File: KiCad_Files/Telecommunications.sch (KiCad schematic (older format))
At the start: 23 parts, among them IC1 L7806ABD2T-TR, J4 CONSMA001-SMD-G, J5 CONSMA001-SMD-G, J6 U_FL-R-SMT_10_, J7 CONSMA001-SMD-G, U2 2AD66-1262, U3 LoRa1262F30, U5 NEO-M8N

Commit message: Add shapes3D folder
Now all 3D models for the components are stored in a single folder, thanks to the Archive Plugin from https://github.com/MitjaNemec/Kicad_action_plugins.git
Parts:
- BT1: symbol Caurin-v.2.0-rescue:ML414H_IV01E-ML414H_IV01E -> archive:Caurin-v.2.0-rescue_ML414H_IV01E-ML414H_IV01E
- C11, C12, C13, C14, C15, C16, C17: symbol Device:C_Small -> archive:Device_C_Small
- D2: symbol Device:D_Schottky_Small -> archive:Device_D_Schottky_Small
- IC1: symbol SamacSys_Parts:L7806ABD2T-TR -> archive:SamacSys_Parts_L7806ABD2T-TR
- J4, J5, J7: symbol dk_Coaxial-Connectors-RF:CONSMA001-SMD-G -> archive:dk_Coaxial-Connectors-RF_CONSMA001-SMD-G
- J6: symbol dk_Coaxial-Connectors-RF:U_FL-R-SMT_10_ -> archive:dk_Coaxial-Connectors-RF_U_FL-R-SMT_10_
- JP2: symbol Jumper:SolderJumper_3_Open -> archive:Jumper_SolderJumper_3_Open
- L1: symbol Device:L_Small -> archive:Device_L_Small
- R5, R6, R7, R8: symbol Device:R_Small -> archive:Device_R_Small
- U2: symbol RF_Modules_Zenith:2AD66-1262 -> archive:RF_Modules_Zenith_2AD66-1262
- U3: symbol RF_Modules_Zenith:LoRa1262F30 -> archive:RF_Modules_Zenith_LoRa1262F30
- U5: symbol Zenith_Modified_Libraries:NEO-M8N -> archive:Zenith_Modified_Libraries_NEO-M8N
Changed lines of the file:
@@
 	9650 4450 9550 4450
 $Comp
-L power:GND #PWR0121
+L archive:power_GND #PWR0121
 U 1 1 60E173C8
 P 8850 5150
@@
 $EndComp
 $Comp
-L power:GND #PWR0122
+L archive:power_GND #PWR0122
 U 1 1 60E17945
 P 9050 2800
@@
 	9050 2700 9050 2800
 $Comp
-L power:+3V3 #PWR0123
+L archive:power_+3V3 #PWR0123
 U 1 1 60E187D2
 P 7700 3150
@@
 $EndComp
 $Comp
-L power:GND #PWR0124
+L archive:power_GND #PWR0124
 U 1 1 60E19D9C
 P 7700 3550
@@
 $EndComp
 $Comp
-L Device:C_Small C15
+L archive:Device_C_Small C15
 U 1 1 60E1A4E4
 P 7700 3400
@@
 NoConn ~ 9550 4150
 $Comp
-L Device:L_Small L1
+L archive:Device_L_Small L1
 U 1 1 60E57109
 P 9875 3375
@@
 	9875 3100 9875 3275
 $Comp
-L Device:R_Small R8
+L archive:Device_R_Small R8
 U 1 1 60E5B23B
 P 9400 3100
@@
 $EndComp
 $Comp
-L Device:C_Small C17
+L archive:Device_C_Small C17
 U 1 1 60E5C8AF
 P 10250 3250
@@
 	4925 3000 4875 3000
 $Comp
-L power:+5V #PWR?
+L archive:power_+5V #PWR?
 U 1 1 60FC2EF1
 P 2600 2050
@@
 	6950 6500 6950 500
 $Comp
-L Caurin-v.2.0-rescue:ML414H_IV01E-ML414H_IV01E BT?
+L archive:Caurin-v.2.0-rescue_ML414H_IV01E-ML414H_IV01E BT?
 U 1 1 6116FC93
 P 8500 2500
@@
 $EndComp
 $Comp
-L Device:C_Small C16
+L archive:Device_C_Small C16
 U 1 1 61171146
 P 8450 2800
@@
 $EndComp
 $Comp
-L Device:R_Small R7
+L archive:Device_R_Small R7
 U 1 1 6117170F
 P 8750 2300
@@
 $EndComp
 $Comp
-L power:+3V3 #PWR0129
+L archive:power_+3V3 #PWR0129
 U 1 1 61172368
 P 8750 1900
@@
 $EndComp
 $Comp
-L power:GND #PWR0130
+L archive:power_GND #PWR0130
 U 1 1 61172B25
 P 8150 2900
@@
 	8750 2500 8700 2500
 $Comp
-L Device:D_Schottky_Small D2
+L archive:Device_D_Schottky_Small D2
 U 1 1 61179C6F
 P 8750 2050
@@
 GPS_TX
 $Comp
-L Device:C_Small C14
+L archive:Device_C_Small C14
 U 1 1 61451F4E
 P 3075 2550
@@
 $EndComp
 $Comp
-L RF_Modules_Zenith:LoRa1262F30 U3
+L archive:RF_Modules_Zenith_LoRa1262F30 U3
 U 1 1 614691E3
 P 4425 2100
@@
 	500  4325 6950 4325
 $Comp
-L RF_Modules_Zenith:2AD66-1262 U2
+L archive:RF_Modules_Zenith_2AD66-1262 U2
 U 1 1 614C66F0
 P 3575 5575
@@
 RADIOS_MISO
 $Comp
-L power:GND #PWR?
+L archive:power_GND #PWR?
 U 1 1 614E9798
 P 3075 2725
@@
 RADIO1_NSS
 $Comp
-L Device:R_Small R5
+L archive:Device_R_Small R5
 U 1 1 61512324
 P 4275 5725
@@
 $EndComp
 $Comp
-L power:+3V3 #PWR0132
+L archive:power_+3V3 #PWR0132
 U 1 1 6151232B
 P 4275 5575
@@
 	4275 5575 4275 5625
 $Comp
-L Device:R_Small R6
+L archive:Device_R_Small R6
 U 1 1 61514E9B
 P 5000 2200
@@
 $EndComp
 $Comp
-L power:+3V3 #PWR0133
+L archive:power_+3V3 #PWR0133
 U 1 1 61514EA2
 P 5000 2075
@@
 	4175 5975 5050 5975
 $Comp
-L Device:C_Small C13
+L archive:Device_C_Small C13
 U 1 1 61544A14
 P 2825 5725
@@
 $EndComp
 $Comp
-L power:GND #PWR?
+L archive:power_GND #PWR?
 U 1 1 61544A1A
 P 2825 5875
@@
 	2825 5825 2825 5875
 $Comp
-L power:+3V3 #PWR0135
+L archive:power_+3V3 #PWR0135
 U 1 1 615473DA
 P 2825 5525
@@
 	3875 2800 3975 2800
 $Comp
-L power:GND #PWR?
+L archive:power_GND #PWR?
 U 1 1 6155871A
 P 4425 3525
@@
 	2975 6275 3075 6275
 $Comp
-L power:GND #PWR?
+L archive:power_GND #PWR?
 U 1 1 6157989A
 P 3625 6975
@@
 	3725 6900 3725 6825
 $Comp
-L SamacSys_Parts:L7806ABD2T-TR IC1
+L archive:SamacSys_Parts_L7806ABD2T-TR IC1
 U 1 1 61E126D4
 P 1975 2875
@@
 $EndComp
 $Comp
-L Device:C_Small C11
+L archive:Device_C_Small C11
 U 1 1 61E1B6CC
 P 1400 3075
@@
 $EndComp
 $Comp
-L Device:C_Small C12
+L archive:Device_C_Small C12
 U 1 1 61E1C718
 P 2600 3075
@@
 $EndComp
 $Comp
-L power:GND #PWR?
+L archive:power_GND #PWR?
 U 1 1 61E1D31F
 P 1975 3375
@@
 	1975 3375 1975 3325
 $Comp
-L Jumper:SolderJumper_3_Open JP2
+L archive:Jumper_SolderJumper_3_Open JP2
 U 1 1 61E5B8C3
 P 2600 2350
@@
 	4175 6375 4225 6375
 $Comp
-L dk_Coaxial-Connectors-RF:CONSMA001-SMD-G J4
+L archive:dk_Coaxial-Connectors-RF_CONSMA001-SMD-G J4
 U 1 1 624D77E2
 P 5200 5875
@@
 $EndComp
 $Comp
-L dk_Coaxial-Connectors-RF:CONSMA001-SMD-G J5
+L archive:dk_Coaxial-Connectors-RF_CONSMA001-SMD-G J5
 U 1 1 624E0650
 P 5875 2350
@@
 $EndComp
 $Comp
-L power:+BATT #PWR0153
+L archive:power_+BATT #PWR0153
 U 1 1 6154AA35
 P 1400 2700
@@
 	1400 2875 1400 2975
 $Comp
-L Zenith_Modified_Libraries:NEO-M8N U5
+L archive:Zenith_Modified_Libraries_NEO-M8N U5
 U 1 1 615EB70D
 P 8850 4150
@@
 	10750 3900 10750 3950
 $Comp
-L dk_Coaxial-Connectors-RF:CONSMA001-SMD-G J7
+L archive:dk_Coaxial-Connectors-RF_CONSMA001-SMD-G J7
 U 1 1 624E5195
 P 10750 4300
@@
 $EndComp
 $Comp
-L dk_Coaxial-Connectors-RF:U_FL-R-SMT_10_ J6
+L archive:dk_Coaxial-Connectors-RF_U_FL-R-SMT_10_ J6
 U 1 1 613F91A3
 P 10750 3700
@@
 	10750 4550 10750 4500
 $Comp
-L power:GNDA #PWR0125
+L archive:power_GNDA #PWR0125
 U 1 1 6160D822
 P 10750 3950
@@
 $EndComp
 $Comp
-L power:GNDA #PWR0126
+L archive:power_GNDA #PWR0126
 U 1 1 6160DC19
 P 10750 4550
@@
 $EndComp
 $Comp
-L power:GNDA #PWR0127
+L archive:power_GNDA #PWR0127
 U 1 1 6160DE64
 P 10250 3400
@@
 $EndComp
 $Comp
-L power:GNDA #PWR0154
+L archive:power_GNDA #PWR0154
 U 1 1 6160E139
 P 9625 3850

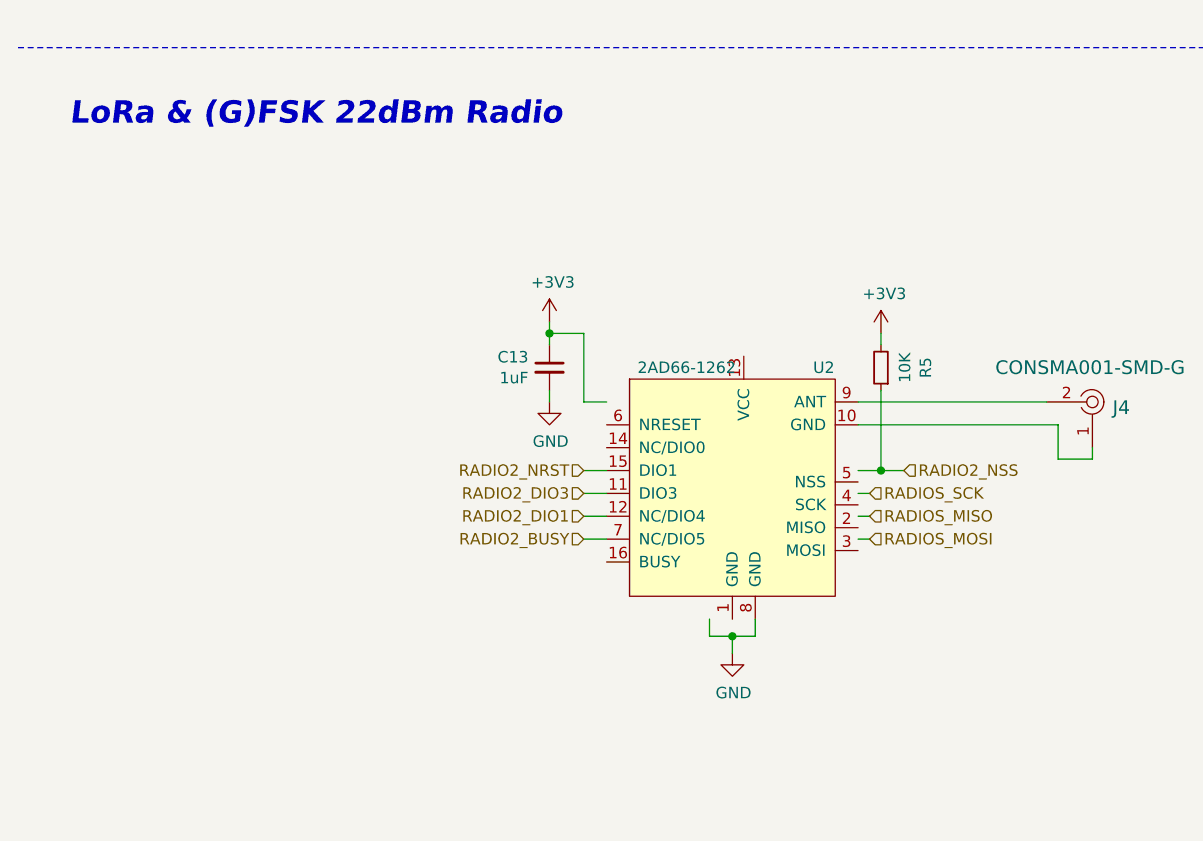
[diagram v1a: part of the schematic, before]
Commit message: Add solder jumper for DIO pins.
Adds solder jumper for DIO pin compatibility between SX1276 and SX1262 low power radios.
Also added the name of the designer (me).
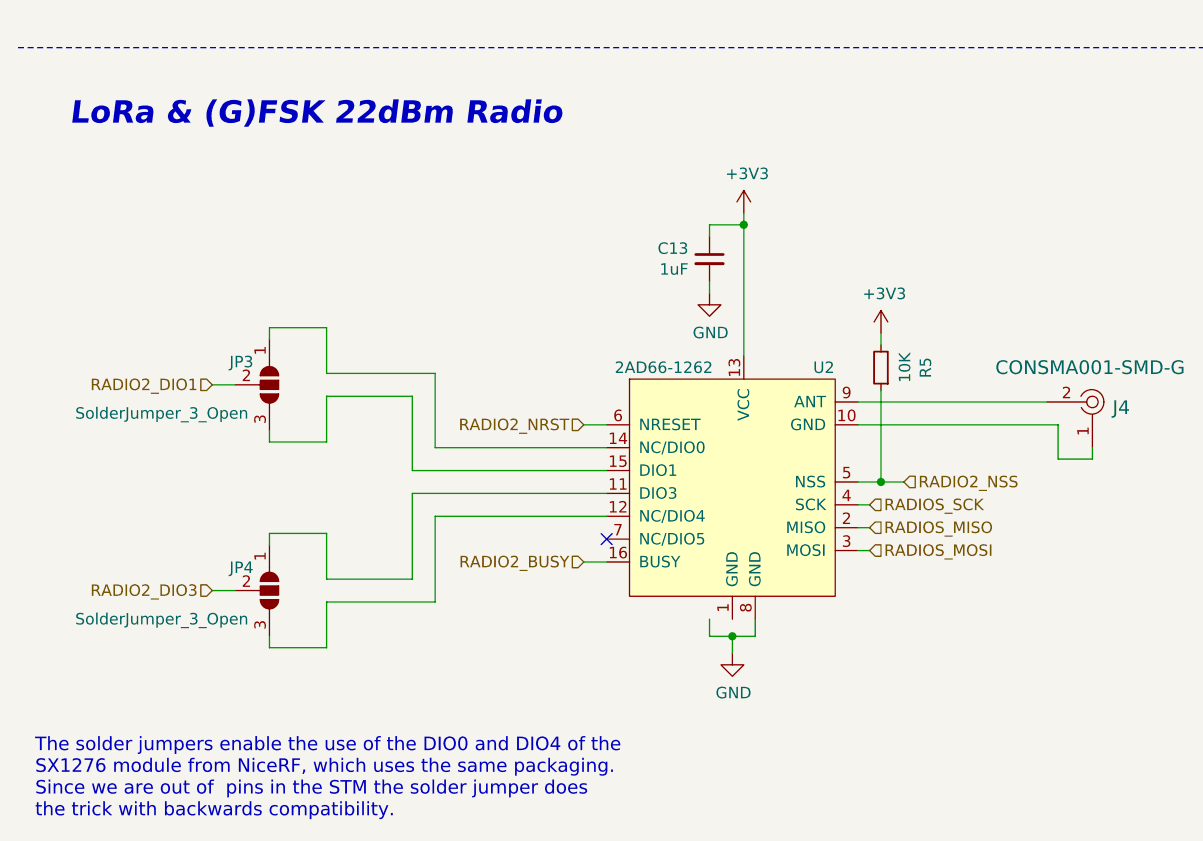
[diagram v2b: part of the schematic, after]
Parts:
- added JP3, JP4: SolderJumper_3_Open, Caurin_Footprints:SolderJumper-3_P1.3mm_Open_RoundedPad1.0x1.5mm_NumberLabels, symbol Jumper:SolderJumper_3_Open
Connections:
- wire segments 113 -> 136
- no-connect marks 7 -> 8
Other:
- note added: "The solder jumpers enable the use of the DIO0 and DIO4 of the\nSX1276 module from NiceRF, which uses the same packaging.\nSince we are out of pins in the STM the solder jumper does\nthe trick with backwards compatibility."
- moved on the sheet: C13
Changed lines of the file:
@@
 Wire Notes Line
 	500  4325 6950 4325
-$Comp
-L archive:RF_Modules_Zenith_2AD66-1262 U2
-U 1 1 614C66F0
-P 3575 5575
-F 0 "U2" H 4025 5425 50  0000 C CNN
-F 1 "2AD66-1262" H 3425 5425 50  0000 C CNN
-F 2 "RF_Modules_Zenith:2AD66-126x" H 3975 5425 50  0001 C CNN
-F 3 "" H 3975 5425 50  0001 C CNN
-	1    3575 5575
-	1    0    0    -1
-$EndComp
 Wire Wire Line
 	4875 2900 4925 2900
 Text HLabel 4925 2900 2    50   Input ~ 0
 RADIOS_MISO
-Text HLabel 4225 6475 2    50   Input ~ 0
+Text HLabel 4225 6525 2    50   Input ~ 0
 RADIOS_MOSI
 Wire Wire Line
-	4225 6475 4175 6475
-Text HLabel 4225 6275 2    50   Input ~ 0
+	4225 6525 4175 6525
+Text HLabel 4225 6325 2    50   Input ~ 0
 RADIOS_SCK
 Wire Wire Line
-	4175 6275 4225 6275
-Text HLabel 4225 6375 2    50   Input ~ 0
+	4175 6325 4225 6325
+Text HLabel 4225 6425 2    50   Input ~ 0
 RADIOS_MISO
 $Comp
@@
 Wire Wire Line
 	5000 2700 5100 2700
-Text HLabel 4375 6175 2    50   Input ~ 0
-RADIO2_NSS
-Wire Wire Line
-	4175 6175 4275 6175
-Wire Wire Line
-	4275 5825 4275 6175
-Wire Wire Line
-	4275 6175 4375 6175
-Connection ~ 4275 6175
-Wire Wire Line
-	5000 5875 4175 5875
 Wire Wire Line
 	5050 5975 5050 6125
@@
 L archive:Device_C_Small C13
 U 1 1 61544A14
-P 2825 5725
-F 0 "C13" H 2917 5771 50  0000 L CNN
-F 1 "1uF" H 2917 5680 50  0000 L CNN
-F 2 "Capacitor_SMD:C_0805_2012Metric" H 2825 5725 50  0001 C CNN
-F 3 "~" H 2825 5725 50  0001 C CNN
-	1    2825 5725
+P 3525 5250
+F 0 "C13" H 3617 5296 50  0000 L CNN
+F 1 "1uF" H 3617 5205 50  0000 L CNN
+F 2 "Capacitor_SMD:C_0805_2012Metric" H 3525 5250 50  0001 C CNN
+F 3 "~" H 3525 5250 50  0001 C CNN
+	1    3525 5250
 	-1   0    0    -1
 $EndComp
@@
 L archive:power_GND #PWR?
 U 1 1 61544A1A
-P 2825 5875
+P 3525 5400
 AR Path="/60D267AF/61544A1A" Ref="#PWR?"  Part="1"
 AR Path="/60D892C4/61544A1A" Ref="#PWR?"  Part="1"
 AR Path="/613F33BD/61544A1A" Ref="#PWR0134"  Part="1"
-F 0 "#PWR0134" H 2825 5625 50  0001 C CNN
-F 1 "GND" H 2830 5702 50  0000 C CNN
-F 2 "" H 2825 5875 50  0001 C CNN
-F 3 "" H 2825 5875 50  0001 C CNN
-	1    2825 5875
-	1    0    0    -1
-$EndComp
-Wire Wire Line
-	2825 5575 2975 5575
-Wire Wire Line
-	2975 5575 2975 5875
-Wire Wire Line
-	2975 5875 3075 5875
-Connection ~ 2825 5575
-Wire Wire Line
-	2825 5575 2825 5625
-Wire Wire Line
-	2825 5825 2825 5875
+F 0 "#PWR0134" H 3525 5150 50  0001 C CNN
+F 1 "GND" H 3530 5227 50  0000 C CNN
+F 2 "" H 3525 5400 50  0001 C CNN
+F 3 "" H 3525 5400 50  0001 C CNN
+	1    3525 5400
+	1    0    0    -1
+$EndComp
+Connection ~ 3675 5100
+Wire Wire Line
+	3675 5100 3525 5100
+Wire Wire Line
+	3525 5350 3525 5400
 $Comp
 L archive:power_+3V3 #PWR0135
 U 1 1 615473DA
-P 2825 5525
-F 0 "#PWR0135" H 2825 5375 50  0001 C CNN
-F 1 "+3V3" H 2840 5698 50  0000 C CNN
-F 2 "" H 2825 5525 50  0001 C CNN
-F 3 "" H 2825 5525 50  0001 C CNN
-	1    2825 5525
-	1    0    0    -1
-$EndComp
-Wire Wire Line
-	2825 5525 2825 5575
+P 3675 5050
+F 0 "#PWR0135" H 3675 4900 50  0001 C CNN
+F 1 "+3V3" H 3690 5223 50  0000 C CNN
+F 2 "" H 3675 5050 50  0001 C CNN
+F 3 "" H 3675 5050 50  0001 C CNN
+	1    3675 5050
+	1    0    0    -1
+$EndComp
+Wire Wire Line
+	3675 5050 3675 5100
 Text HLabel 3875 3000 0    50   Input ~ 0
 RADIO1_DIO3
@@
 	4475 3475 4475 3400
 Connection ~ 4425 3475
-Text HLabel 2975 6375 0    50   Input ~ 0
+Text HLabel 1350 5800 0    50   Input ~ 0
 RADIO2_DIO1
 Wire Wire Line
-	2975 6375 3075 6375
-Text HLabel 2975 6275 0    50   Input ~ 0
+	1350 5800 1450 5800
+Text HLabel 1350 6700 0    50   Input ~ 0
 RADIO2_DIO3
 Wire Wire Line
-	2975 6475 3075 6475
-Text HLabel 2975 6175 0    50   Input ~ 0
+	2975 6575 3075 6575
+Text HLabel 2975 5975 0    50   Input ~ 0
 RADIO2_NRST
 Wire Wire Line
-	2975 6175 3075 6175
-Text HLabel 2975 6475 0    50   Input ~ 0
+	2975 5975 3075 5975
+Text HLabel 2975 6575 0    50   Input ~ 0
 RADIO2_BUSY
-Wire Wire Line
-	2975 6275 3075 6275
 $Comp
 L archive:power_GND #PWR?
@@
 	3625 6900 3725 6900
 Wire Wire Line
-	4175 6375 4225 6375
+	4175 6425 4225 6425
 $Comp
 L archive:dk_Coaxial-Connectors-RF_CONSMA001-SMD-G J4
@@
 EndData
 $EndBitmap
+Wire Wire Line
+	3525 5100 3525 5150
+Wire Wire Line
+	3675 5100 3675 5675
+$Comp
+L archive:RF_Modules_Zenith_2AD66-1262 U2
+U 1 1 614C66F0
+P 3575 5575
+F 0 "U2" H 4025 5425 50  0000 C CNN
+F 1 "2AD66-1262" H 3325 5425 50  0000 C CNN
+F 2 "RF_Modules_Zenith:2AD66-126x" H 3975 5425 50  0001 C CNN
+F 3 "" H 3975 5425 50  0001 C CNN
+	1    3575 5575
+	1    0    0    -1
+$EndComp
+NoConn ~ 3075 6475
+$Comp
+L Jumper:SolderJumper_3_Open JP3
+U 1 1 62D44341
+P 1600 5800
+F 0 "JP3" V 1500 5625 50  0000 L CNN
+F 1 "SolderJumper_3_Open" V 1725 4950 50  0000 L CNN
+F 2 "Caurin_Footprints:SolderJumper-3_P1.3mm_Open_RoundedPad1.0x1.5mm_NumberLabels" H 1600 5800 50  0001 C CNN
+F 3 "~" H 1600 5800 50  0001 C CNN
+	1    1600 5800
+	0    1    1    0
+$EndComp
+Wire Wire Line
+	1600 5600 1600 5550
+Wire Wire Line
+	1600 5550 1850 5550
+Wire Wire Line
+	1850 5550 1850 5750
+Wire Wire Line
+	1850 5850 1850 6050
+Wire Wire Line
+	1600 6050 1600 6000
+Wire Wire Line
+	1850 6050 1600 6050
+Text Notes 575  7700 0    59   ~ 0
+The solder jumpers enable the use of the DIO0 and DIO4 of the\nSX1276 module from NiceRF, which uses the same packaging.\nSince we are out of  pins in the STM the solder jumper does\nthe trick with backwards compatibility.
+Wire Wire Line
+	1350 6700 1450 6700
+$Comp
+L Jumper:SolderJumper_3_Open JP4
+U 1 1 62D9AB35
+P 1600 6700
+F 0 "JP4" V 1500 6525 50  0000 L CNN
+F 1 "SolderJumper_3_Open" V 1725 5850 50  0000 L CNN
+F 2 "Caurin_Footprints:SolderJumper-3_P1.3mm_Open_RoundedPad1.0x1.5mm_NumberLabels" H 1600 6700 50  0001 C CNN
+F 3 "~" H 1600 6700 50  0001 C CNN
+	1    1600 6700
+	0    1    1    0
+$EndComp
+Wire Wire Line
+	1600 6500 1600 6450
+Wire Wire Line
+	1600 6450 1850 6450
+Wire Wire Line
+	1850 6450 1850 6650
+Wire Wire Line
+	1850 6750 1850 6950
+Wire Wire Line
+	1600 6950 1600 6900
+Wire Wire Line
+	1850 6950 1600 6950
+Wire Wire Line
+	2225 6650 2225 6275
+Wire Wire Line
+	2225 6275 3075 6275
+Wire Wire Line
+	2325 6750 2325 6375
+Wire Wire Line
+	2325 6375 3075 6375
+Wire Wire Line
+	1850 6650 2225 6650
+Wire Wire Line
+	2325 6750 1850 6750
+Wire Wire Line
+	1850 5850 2225 5850
+Wire Wire Line
+	2225 5850 2225 6175
+Wire Wire Line
+	2225 6175 3075 6175
+Wire Wire Line
+	3075 6075 2325 6075
+Wire Wire Line
+	2325 6075 2325 5750
+Wire Wire Line
+	2325 5750 1850 5750
+Wire Wire Line
+	5000 5875 4175 5875
+Connection ~ 4275 6225
+Wire Wire Line
+	4275 6225 4375 6225
+Wire Wire Line
+	4275 5825 4275 6225
+Wire Wire Line
+	4175 6225 4275 6225
+Text HLabel 4375 6225 2    50   Input ~ 0
+RADIO2_NSS
 $EndSCHEMATC
